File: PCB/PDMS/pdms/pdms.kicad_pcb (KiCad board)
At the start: 2 copper layers, 166 parts, among them IC1 BTS500101TAEATMA1, IC10 LDO40LPU50RY, IC11 MP2332HGTL-P, IC12 TMP126NDCKR, IC14 TMP126NDCKR, IC15 LM74700MDDFREP, IC16 BTS722204ESAXUMA1, IC19 STM32L496ZGT6, IC2 BTS500101TAEATMA1, IC20 AT25SF128A-SHB-T, IC3 BTS500101TAEATMA1, IC4 BTS500101TAEATMA1, IC5 BTS500101TAEATMA1, IC6 BTS500101TAEATMA1, IC7 BTS722204ESAXUMA1, IC8 BTS500101TAEATMA1, IC9 BTS500101TAEATMA1, J1 DBG, Q1 AO3401A, Q2 MMBT3904, Q3 IAUA250N04S6N007AUMA1, U1 CPC1117N, U2 MCP2561-E-SN, U3 MCP2561-E-SN, Y1 48Mhz, Y2 32KHz

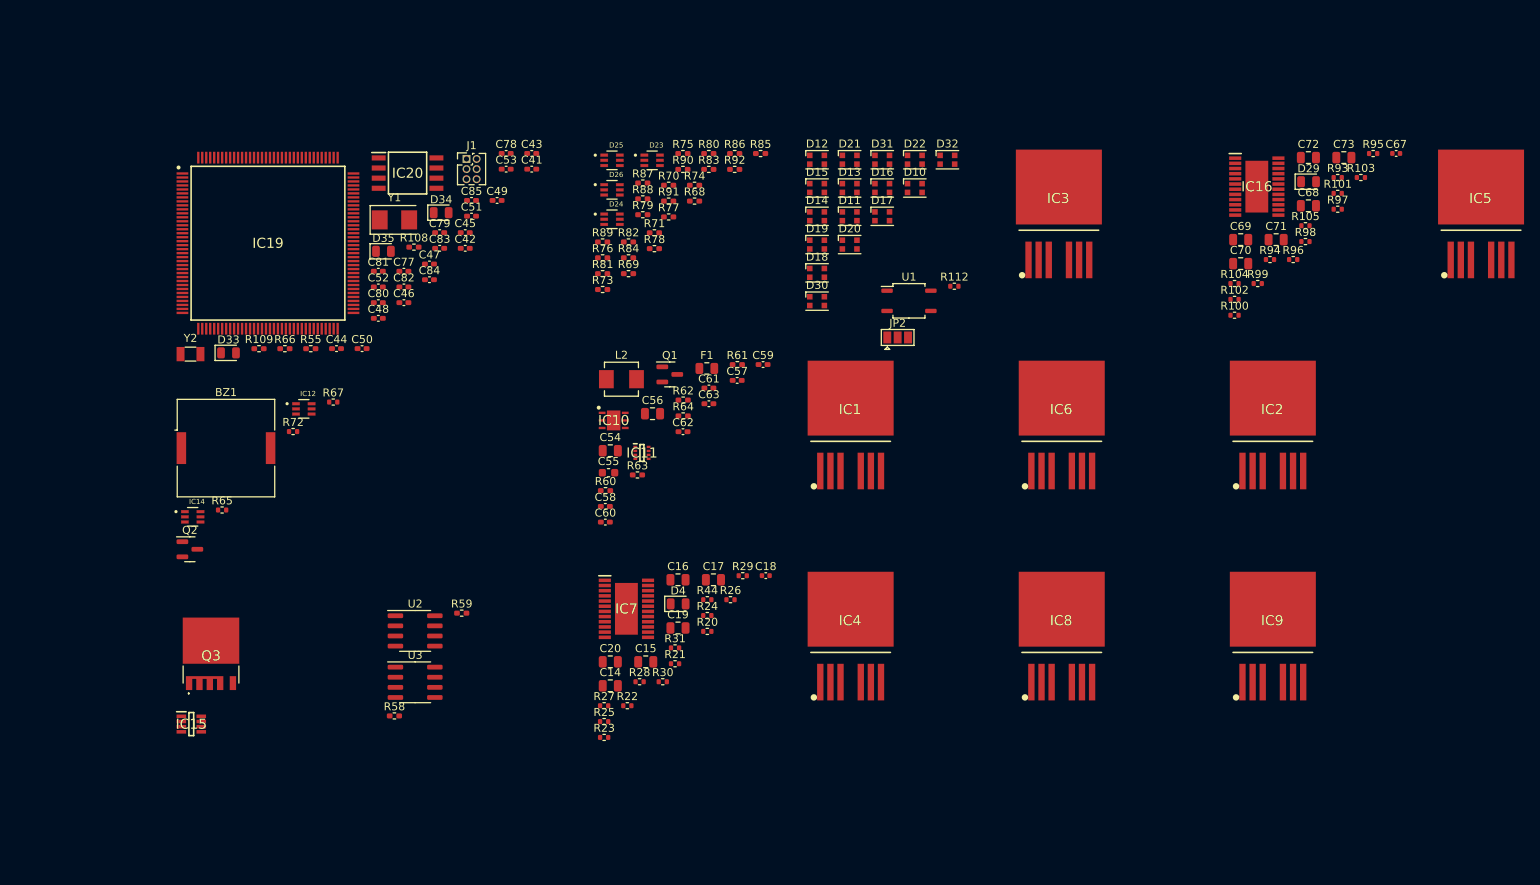
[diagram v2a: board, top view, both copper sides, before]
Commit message: Mostly assigned footprints
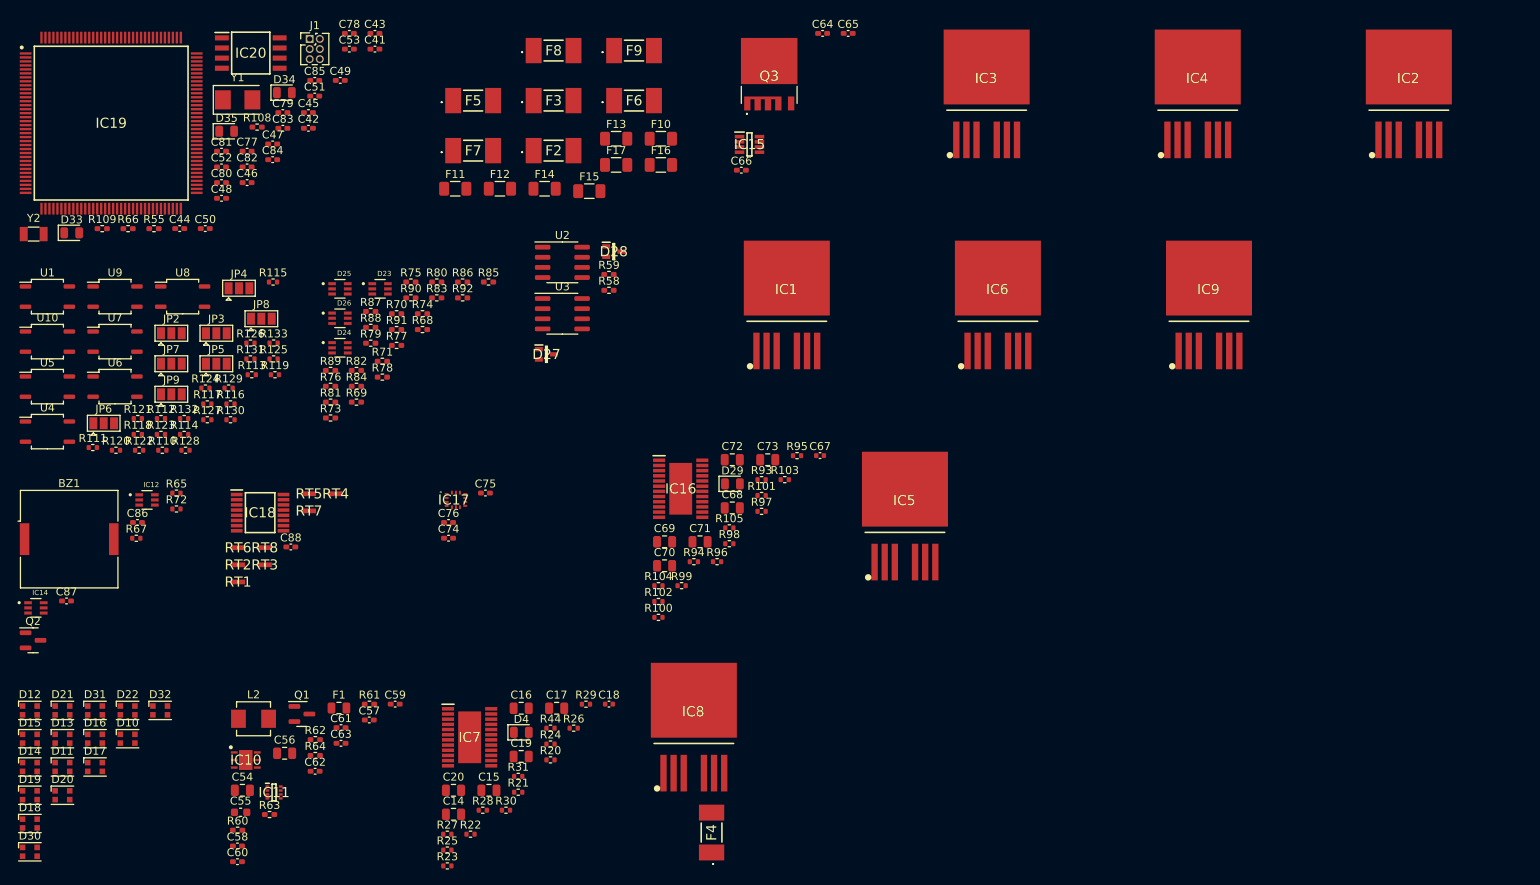
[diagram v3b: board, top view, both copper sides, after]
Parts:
- added C64: 22uF, Capacitor_SMD:C_0402_1005Metric_Pad0.74x0.62mm_HandSolder, F.Cu at (176.5, 69.9)
- added C65: 0.1uF, Capacitor_SMD:C_0402_1005Metric_Pad0.74x0.62mm_HandSolder, F.Cu at (179.7, 69.9)
- added C66: 100nF, Capacitor_SMD:C_0402_1005Metric_Pad0.74x0.62mm_HandSolder, F.Cu at (166.3, 87.0)
- added C74: 100nF, Capacitor_SMD:C_0402_1005Metric_Pad0.74x0.62mm_HandSolder, F.Cu at (129.5, 133.2)
- added C75: 10nF, Capacitor_SMD:C_0402_1005Metric_Pad0.74x0.62mm_HandSolder, F.Cu at (134.2, 127.6)
- added C76: 100nF, Capacitor_SMD:C_0402_1005Metric_Pad0.74x0.62mm_HandSolder, F.Cu at (129.5, 131.3)
- added C86: 0.1uF, Capacitor_SMD:C_0402_1005Metric_Pad0.74x0.62mm_HandSolder, F.Cu at (90.5, 131.3)
- added C87: 0.1uF, Capacitor_SMD:C_0402_1005Metric_Pad0.74x0.62mm_HandSolder, F.Cu at (81.6, 141.1)
- added C88: 100nF, Capacitor_SMD:C_0402_1005Metric_Pad0.74x0.62mm_HandSolder, F.Cu at (109.7, 134.3)
- added D27: PESD2CANFD24L-UX, PDMS_Additional:SOT65P210X110-3N, F.Cu at (141.8, 110.2)
- added D28: PESD2CANFD24L-UX, PDMS_Additional:SOT65P210X110-3N, F.Cu at (150.3, 97.2)
- added F10: 7A, Fuse:Fuse_1206_3216Metric, F.Cu at (156.2, 83.1)
- added F11: 7A, Fuse:Fuse_1206_3216Metric, F.Cu at (130.4, 89.4)
- added F12: 7A, Fuse:Fuse_1206_3216Metric, F.Cu at (136.0, 89.4)
- added F13: 7A, Fuse:Fuse_1206_3216Metric, F.Cu at (150.6, 83.1)
- added F14: 7A, Fuse:Fuse_1206_3216Metric, F.Cu at (141.6, 89.4)
- added F15: 7A, Fuse:Fuse_1206_3216Metric, F.Cu at (147.2, 89.7)
- added F16: 7A, Fuse:Fuse_1206_3216Metric, F.Cu at (156.2, 86.4)
- added F17: 7A, Fuse:Fuse_1206_3216Metric, F.Cu at (150.6, 86.4)
- added F2: 40A, PDMS_Additional:0ACA9400TE, F.Cu at (142.7, 84.6)
- added F3: 40A, PDMS_Additional:0ACA9400TE, F.Cu at (142.7, 78.3)
- added F4: 40A, PDMS_Additional:0ACA9400TE, F.Cu at (162.6, 170.2)
- added F5: 40A, PDMS_Additional:0ACA9400TE, F.Cu at (132.6, 78.3)
- added F6: 40A, PDMS_Additional:0ACA9400TE, F.Cu at (152.8, 78.3)
- added F7: 40A, PDMS_Additional:0ACA9400TE, F.Cu at (132.6, 84.6)
- added F8: 40A, PDMS_Additional:0ACA9400TE, F.Cu at (142.7, 72.0)
- added F9: 40A, PDMS_Additional:0ACA9400TE, F.Cu at (152.8, 72.0)
- added IC17: ASM330LHHTR, PDMS_Additional:LGA-14_2.5X3X0.86_, F.Cu at (130.5, 128.4)
- added IC18: NX3L4051PW,118, PDMS_Additional:SOP65P640X110-16N, F.Cu at (105.9, 130.0)
- added JP3: IN_SEL, Jumper:SolderJumper-3_P1.3mm_Open_Pad1.0x1.5mm, F.Cu at (100.4, 107.5)
- added JP4: IN_SEL, Jumper:SolderJumper-3_P1.3mm_Open_Pad1.0x1.5mm, F.Cu at (103.2, 101.8)
- added JP5: IN_SEL, Jumper:SolderJumper-3_P1.3mm_Open_Pad1.0x1.5mm, F.Cu at (100.4, 111.3)
- added JP6: IN_SEL, Jumper:SolderJumper-3_P1.3mm_Open_Pad1.0x1.5mm, F.Cu at (86.2, 118.8)
- added JP7: IN_SEL, Jumper:SolderJumper-3_P1.3mm_Open_Pad1.0x1.5mm, F.Cu at (94.7, 111.3)
- added JP8: IN_SEL, Jumper:SolderJumper-3_P1.3mm_Open_Pad1.0x1.5mm, F.Cu at (106.0, 105.7)
- added JP9: IN_SEL, Jumper:SolderJumper-3_P1.3mm_Open_Pad1.0x1.5mm, F.Cu at (94.7, 115.2)
- added R110: 0Ohm, Resistor_SMD:R_0402_1005Metric, F.Cu at (93.6, 122.2)
- added R111: 0Ohm, Resistor_SMD:R_0402_1005Metric, F.Cu at (84.9, 121.8)
- added R113: 0Ohm, Resistor_SMD:R_0402_1005Metric, F.Cu at (104.8, 112.7)
- added R114: 0Ohm, Resistor_SMD:R_0402_1005Metric, F.Cu at (96.3, 120.2)
- added R115: 0Ohm, Resistor_SMD:R_0402_1005Metric, F.Cu at (107.5, 101.1)
- added R116: 0Ohm, Resistor_SMD:R_0402_1005Metric, F.Cu at (102.2, 116.4)
- added R117: 0Ohm, Resistor_SMD:R_0402_1005Metric, F.Cu at (99.3, 116.4)
- added R118: 0Ohm, Resistor_SMD:R_0402_1005Metric, F.Cu at (90.5, 120.2)
- added R119: 0Ohm, Resistor_SMD:R_0402_1005Metric, F.Cu at (107.8, 112.7)
- added R120: 0Ohm, Resistor_SMD:R_0402_1005Metric, F.Cu at (87.8, 122.2)
- added R121: 0Ohm, Resistor_SMD:R_0402_1005Metric, F.Cu at (90.5, 118.2)
- added R122: 0Ohm, Resistor_SMD:R_0402_1005Metric, F.Cu at (90.7, 122.2)
- added R123: 0Ohm, Resistor_SMD:R_0402_1005Metric, F.Cu at (93.4, 120.2)
- added R124: 0Ohm, Resistor_SMD:R_0402_1005Metric, F.Cu at (99.0, 114.4)
- added R125: 0Ohm, Resistor_SMD:R_0402_1005Metric, F.Cu at (107.6, 110.7)
- added R126: 0Ohm, Resistor_SMD:R_0402_1005Metric, F.Cu at (104.7, 108.7)
- added R127: 1k, Resistor_SMD:R_0402_1005Metric, F.Cu at (99.3, 118.4)
- added R128: 1k, Resistor_SMD:R_0402_1005Metric, F.Cu at (96.5, 122.2)
- added R129: 1k, Resistor_SMD:R_0402_1005Metric, F.Cu at (101.9, 114.4)
- added R130: 1k, Resistor_SMD:R_0402_1005Metric, F.Cu at (102.2, 118.4)
- added R131: 1k, Resistor_SMD:R_0402_1005Metric, F.Cu at (104.7, 110.7)
- added R132: 1k, Resistor_SMD:R_0402_1005Metric, F.Cu at (96.3, 118.2)
- added R133: 1k, Resistor_SMD:R_0402_1005Metric, F.Cu at (107.6, 108.7)
- added RT1: B57232V5103F360, PDMS_Additional:THRMC1005X60N, F.Cu at (103.1, 138.7)
- added RT2: B57232V5103F360, PDMS_Additional:THRMC1005X60N, F.Cu at (103.1, 136.6)
- added RT3: B57232V5103F360, PDMS_Additional:THRMC1005X60N, F.Cu at (106.5, 136.6)
- added RT4: B57232V5103F360, PDMS_Additional:THRMC1005X60N, F.Cu at (115.4, 127.7)
- added RT5: B57232V5103F360, PDMS_Additional:THRMC1005X60N, F.Cu at (112.0, 127.7)
- added RT6: B57232V5103F360, PDMS_Additional:THRMC1005X60N, F.Cu at (103.1, 134.4)
- added RT7: B57232V5103F360, PDMS_Additional:THRMC1005X60N, F.Cu at (112.0, 129.8)
- added RT8: B57232V5103F360, PDMS_Additional:THRMC1005X60N, F.Cu at (106.5, 134.4)
- added U10: CPC1117N, Package_SO:SOP-4_3.8x4.1mm_P2.54mm, F.Cu at (79.2, 108.5)
- added U4: CPC1117N, Package_SO:SOP-4_3.8x4.1mm_P2.54mm, F.Cu at (79.2, 119.8)
- added U5: CPC1117N, Package_SO:SOP-4_3.8x4.1mm_P2.54mm, F.Cu at (79.2, 114.2)
- added U6: CPC1117N, Package_SO:SOP-4_3.8x4.1mm_P2.54mm, F.Cu at (87.7, 114.2)
- added U7: CPC1117N, Package_SO:SOP-4_3.8x4.1mm_P2.54mm, F.Cu at (87.7, 108.5)
- added U8: CPC1117N, Package_SO:SOP-4_3.8x4.1mm_P2.54mm, F.Cu at (96.2, 102.9)
- added U9: CPC1117N, Package_SO:SOP-4_3.8x4.1mm_P2.54mm, F.Cu at (87.7, 102.9)
- C14, C15, C16, C17, C70, C71, C72, C73: value 10nf -> 10nF
- F1: value Fuse -> 3A
- moved D11 120.6 mm to (81.1, 161.9)
- moved D13 120.6 mm to (81.1, 158.4)
- moved D16 120.6 mm to (85.2, 158.4)
- moved D17 120.6 mm to (85.2, 161.9)
- moved D20 120.6 mm to (81.1, 165.5)
- moved D21 120.6 mm to (81.1, 154.8)
- moved D31 120.6 mm to (85.2, 154.8)
- moved D12 120.6 mm to (77.0, 154.8)
- moved D14 120.6 mm to (77.0, 161.9)
- moved D15 120.6 mm to (77.0, 158.4)
- moved D18 120.6 mm to (77.0, 169.1)
- moved D19 120.6 mm to (77.0, 165.5)
- moved D30 120.6 mm to (77.0, 172.6)
- moved D10 120.6 mm to (89.2, 158.4)
- moved D22 120.6 mm to (89.2, 154.8)
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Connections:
- net CONN_INPUT1 renamed CONN_AD_IN1
- C54 pad 1: +12V -> 12V_LOGIC_ONLY
- C56 pad 2: +12V -> 12V_LOGIC_ONLY
- C58 pad 2: +12V -> 12V_LOGIC_ONLY
- F1 pad 1: Net-(F1-Pad1) -> 12V_LOGIC_ONLY
- IC10 pad 2: +12V -> 12V_LOGIC_ONLY
- IC10 pad 3: +12V -> 12V_LOGIC_ONLY
- IC11 pad 2: +12V -> 12V_LOGIC_ONLY
- IC12 pad 6: VDD -> Net-(C86-Pad1)
- IC14 pad 5: /PERIPHERAL/TEMP2_ALERT -> /PERIPHERAL/TEMP1_ALERT
- IC14 pad 6: VDD -> Net-(C87-Pad1)
- IC15 pad 1: /REVERSE_POLARITY_PROT/IN -> 12V_CONN
- IC15 pad 5: /REVERSE_POLARITY_PROT/IN -> 12V_CONN
- IC19 pad 118: /PERIPHERAL/TEMP2_ALERT -> /TEMP2_ALERT
- Q3 pad 1: /REVERSE_POLARITY_PROT/IN -> 12V_CONN
- Q3 pad 2: /REVERSE_POLARITY_PROT/IN -> 12V_CONN
- Q3 pad 3: /REVERSE_POLARITY_PROT/IN -> 12V_CONN
- Q3 pad 4: /REVERSE_POLARITY_PROT/IN -> 12V_CONN
- Q3 pad 7: /REVERSE_POLARITY_PROT/IN -> 12V_CONN
- R60 pad 2: +12V -> 12V_LOGIC_ONLY
- R67 pad 1: /PERIPHERAL/TEMP2_ALERT -> VDD
- R67 pad 2: VDD -> /PERIPHERAL/TEMP1_ALERT
- U1 pad 4: SIG_IN[1..8] -> SIG_IN1

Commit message: Crucial fully assigned schematics
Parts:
- added C1: 10nF, Capacitor_SMD:C_0402_1005Metric, F.Cu at (60.0, 91.2)
- added C10: 150nF, Capacitor_SMD:C_0805_2012Metric, F.Cu at (114.7, 31.0)
- added C11: 100nF, Capacitor_SMD:C_0805_2012Metric, F.Cu at (106.7, 32.5)
- added C12: 10nF, Capacitor_SMD:C_0805_2012Metric, F.Cu at (114.7, 28.0)
- added C13: 10nF, Capacitor_SMD:C_0402_1005Metric, F.Cu at (98.2, 64.7)
- added C2: 150nF, Capacitor_SMD:C_0805_2012Metric, F.Cu at (61.5, 88.7)
- added C21: 150nF, Capacitor_SMD:C_0805_2012Metric, F.Cu at (99.7, 62.2)
- added C22: 100nF, Capacitor_SMD:C_0805_2012Metric, F.Cu at (91.6, 63.8)
- added C23: 10nF, Capacitor_SMD:C_0805_2012Metric, F.Cu at (99.7, 59.2)
- added C24: 10nF, Capacitor_SMD:C_0402_1005Metric, F.Cu at (60.0, 117.7)
- added C25: 150nF, Capacitor_SMD:C_0805_2012Metric, F.Cu at (61.5, 115.2)
- added C26: 100nF, Capacitor_SMD:C_0805_2012Metric, F.Cu at (53.5, 116.8)
- added C27: 10nF, Capacitor_SMD:C_0805_2012Metric, F.Cu at (61.5, 112.2)
- added C28: 10nF, Capacitor_SMD:C_0402_1005Metric, F.Cu at (142.4, 33.5)
- added C29: 150nF, Capacitor_SMD:C_0805_2012Metric, F.Cu at (143.9, 31.0)
- added C3: 100nF, Capacitor_SMD:C_0805_2012Metric, F.Cu at (53.5, 90.3)
- added C30: 100nF, Capacitor_SMD:C_0805_2012Metric, F.Cu at (135.8, 32.5)
- added C31: 10nF, Capacitor_SMD:C_0805_2012Metric, F.Cu at (143.9, 28.0)
- added C32: 10nF, Capacitor_SMD:C_0402_1005Metric, F.Cu at (89.2, 91.2)
- added C33: 150nF, Capacitor_SMD:C_0805_2012Metric, F.Cu at (90.7, 88.7)
- added C34: 100nF, Capacitor_SMD:C_0805_2012Metric, F.Cu at (82.6, 90.3)
- added C35: 10nF, Capacitor_SMD:C_0805_2012Metric, F.Cu at (90.7, 85.7)
- added C36: 10nF, Capacitor_SMD:C_0402_1005Metric, F.Cu at (171.5, 33.5)
- added C37: 150nF, Capacitor_SMD:C_0805_2012Metric, F.Cu at (173.0, 31.0)
- added C38: 100nF, Capacitor_SMD:C_0805_2012Metric, F.Cu at (165.0, 32.5)
- added C39: 10nF, Capacitor_SMD:C_0805_2012Metric, F.Cu at (173.0, 28.0)
- added C4: 10nF, Capacitor_SMD:C_0805_2012Metric, F.Cu at (61.5, 85.7)
- added C5: 10nF, Capacitor_SMD:C_0402_1005Metric, F.Cu at (127.3, 60.0)
- added C6: 150nF, Capacitor_SMD:C_0805_2012Metric, F.Cu at (128.8, 57.5)
- added C7: 100nF, Capacitor_SMD:C_0805_2012Metric, F.Cu at (120.8, 59.0)
- added C8: 10nF, Capacitor_SMD:C_0805_2012Metric, F.Cu at (128.8, 54.5)
- added C9: 10nF, Capacitor_SMD:C_0402_1005Metric, F.Cu at (113.2, 33.5)
- added D1: 40V, Diode_SMD:D_SMA, F.Cu at (55.3, 86.5)
- added D2: 40V, Diode_SMD:D_SMA, F.Cu at (122.6, 55.2)
- added D3: 40V, Diode_SMD:D_SMA, F.Cu at (108.5, 28.7)
- added D5: 40V, Diode_SMD:D_SMA, F.Cu at (93.4, 60.0)
- added D6: 40V, Diode_SMD:D_SMA, F.Cu at (55.3, 113.0)
- added D7: 40V, Diode_SMD:D_SMA, F.Cu at (137.6, 28.7)
- added D8: 40V, Diode_SMD:D_SMA, F.Cu at (84.4, 86.5)
- added D9: 40V, Diode_SMD:D_SMA, F.Cu at (166.8, 28.7)
- added JP1: SolderJumper_3_Open, Jumper:SolderJumper-3_P1.3mm_Open_Pad1.0x1.5mm, F.Cu at (66.8, 40.0)
- added R1: 4.7k, Resistor_SMD:R_0402_1005Metric, F.Cu at (57.1, 91.7)
- added R10: 1k, Resistor_SMD:R_0805_2012Metric, F.Cu at (120.8, 62.0)
- added R106: 20k, Resistor_SMD:R_0402_1005Metric, F.Cu at (96.5, 124.9)
- added R107: 10, Resistor_SMD:R_0402_1005Metric, F.Cu at (105.4, 116.0)
- added R11: 4.7k, Resistor_SMD:R_0402_1005Metric, F.Cu at (110.3, 34.0)
- added R12: 4.7k, Resistor_SMD:R_0402_1005Metric, F.Cu at (105.9, 38.0)
- added R13: 4.7k, Resistor_SMD:R_0402_1005Metric, F.Cu at (110.3, 32.0)
- added R14: 4.7k, Resistor_SMD:R_0402_1005Metric, F.Cu at (104.2, 44.6)
- added R15: 1k, Resistor_SMD:R_0805_2012Metric, F.Cu at (106.6, 35.5)
- added R16: 4.7k, Resistor_SMD:R_0402_1005Metric, F.Cu at (95.3, 65.2)
- added R17: 4.7k, Resistor_SMD:R_0402_1005Metric, F.Cu at (90.9, 69.2)
- added R18: 4.7k, Resistor_SMD:R_0402_1005Metric, F.Cu at (95.3, 63.2)
- added R19: 4.7k, Resistor_SMD:R_0402_1005Metric, F.Cu at (89.2, 75.9)
- added R2: 4.7k, Resistor_SMD:R_0402_1005Metric, F.Cu at (52.7, 95.7)
- added R3: 4.7k, Resistor_SMD:R_0402_1005Metric, F.Cu at (57.1, 89.7)
- added R32: 1k, Resistor_SMD:R_0805_2012Metric, F.Cu at (91.6, 66.7)
- added R33: 4.7k, Resistor_SMD:R_0402_1005Metric, F.Cu at (57.1, 118.2)
- added R34: 4.7k, Resistor_SMD:R_0402_1005Metric, F.Cu at (52.7, 122.2)
- added R35: 4.7k, Resistor_SMD:R_0402_1005Metric, F.Cu at (57.1, 116.2)
- added R36: 4.7k, Resistor_SMD:R_0402_1005Metric, F.Cu at (51.0, 128.9)
- added R37: 1k, Resistor_SMD:R_0805_2012Metric, F.Cu at (53.4, 119.7)
- added R38: 4.7k, Resistor_SMD:R_0402_1005Metric, F.Cu at (139.5, 34.0)
- added R39: 4.7k, Resistor_SMD:R_0402_1005Metric, F.Cu at (135.0, 38.0)
- added R4: 4.7k, Resistor_SMD:R_0402_1005Metric, F.Cu at (51.0, 102.4)
- added R40: 4.7k, Resistor_SMD:R_0402_1005Metric, F.Cu at (139.5, 32.0)
- added R41: 4.7k, Resistor_SMD:R_0402_1005Metric, F.Cu at (133.3, 44.6)
- added R42: 1k, Resistor_SMD:R_0805_2012Metric, F.Cu at (135.8, 35.5)
- added R43: 4.7k, Resistor_SMD:R_0402_1005Metric, F.Cu at (86.3, 91.7)
- added R45: 4.7k, Resistor_SMD:R_0402_1005Metric, F.Cu at (81.8, 95.7)
- added R46: 4.7k, Resistor_SMD:R_0402_1005Metric, F.Cu at (86.3, 89.7)
- added R47: 4.7k, Resistor_SMD:R_0402_1005Metric, F.Cu at (80.1, 102.4)
- added R48: 1k, Resistor_SMD:R_0805_2012Metric, F.Cu at (82.6, 93.2)
- added R49: 4.7k, Resistor_SMD:R_0402_1005Metric, F.Cu at (168.6, 34.0)
- added R5: 1k, Resistor_SMD:R_0805_2012Metric, F.Cu at (53.4, 93.2)
- added R50: 4.7k, Resistor_SMD:R_0402_1005Metric, F.Cu at (164.2, 38.0)
- added R51: 4.7k, Resistor_SMD:R_0402_1005Metric, F.Cu at (168.6, 32.0)
- added R52: 4.7k, Resistor_SMD:R_0402_1005Metric, F.Cu at (162.5, 44.6)
- added R53: 1k, Resistor_SMD:R_0805_2012Metric, F.Cu at (164.9, 35.5)
- added R6: 4.7k, Resistor_SMD:R_0402_1005Metric, F.Cu at (124.5, 60.5)
- added R7: 4.7k, Resistor_SMD:R_0402_1005Metric, F.Cu at (120.0, 64.5)
- added R8: 4.7k, Resistor_SMD:R_0402_1005Metric, F.Cu at (124.5, 58.5)
- added R9: 4.7k, Resistor_SMD:R_0402_1005Metric, F.Cu at (118.3, 71.1)
- moved C16 149.0 mm to (217.3, 28.0)
- moved C18 149.0 mm to (228.3, 27.5)
- moved R20 149.0 mm to (221.0, 34.5)
- moved R21 149.0 mm to (216.9, 38.5)
- moved R23 149.0 mm to (208.0, 47.8)
- moved R26 149.0 mm to (223.9, 30.5)
- moved R44 149.0 mm to (221.0, 30.5)
- moved C14 149.0 mm to (208.8, 41.3)
- moved C15 149.0 mm to (213.3, 38.3)
- moved C17 149.0 mm to (221.8, 28.0)
- moved C19 149.0 mm to (217.3, 34.0)
- moved C20 149.0 mm to (208.8, 38.3)
- moved D4 149.0 mm to (217.3, 31.0)
- moved IC7 149.0 mm to (210.8, 31.6)
- moved R22 149.0 mm to (210.9, 43.8)
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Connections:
- net /POWER_SWITCHES/BTS50010-1TAE/MOS_OUT renamed Net-(C4-Pad1)
- net /POWER_SWITCHES/BTS50010-1TAE1/MOS_OUT renamed Net-(C8-Pad1)
- net /POWER_SWITCHES/BTS50010-1TAE2/MOS_OUT renamed Net-(C12-Pad1)
- net /POWER_SWITCHES/BTS50010-1TAE3/MOS_OUT renamed Net-(C23-Pad1)
- net /POWER_SWITCHES/BTS50010-1TAE4/MOS_OUT renamed Net-(C27-Pad1)
- net /POWER_SWITCHES/BTS50010-1TAE5/MOS_OUT renamed Net-(C39-Pad1)
- net /POWER_SWITCHES/BTS50010-1TAE6/MOS_OUT renamed Net-(C31-Pad1)
- net /POWER_SWITCHES/BTS50010-1TAE7/MOS_OUT renamed Net-(C35-Pad1)

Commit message: Added connector and more
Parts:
- added J2: 6473427-1, PDMS_Additional:64734271, F.Cu at (112.1, 52.6)
- added L1: 2u7 120m, Inductor_SMD:L_0402_1005Metric, F.Cu at (69.8, 131.2)
- added R54: 0, Resistor_SMD:R_0805_2012Metric, F.Cu at (68.6, 126.8)
- added R56: 10k, Resistor_SMD:R_0402_1005Metric, F.Cu at (38.9, 176.6)
- added R57: 10k, Resistor_SMD:R_0402_1005Metric, F.Cu at (52.9, 160.5)
- C41, C42, C43, C44, C45, C46, C47, C48, C49, C50, C51, C52, C53, C57, C58, C59, C60, C61, C62, C63, C65: footprint Capacitor_SMD:C_0402_1005Metric_Pad0.74x0.62mm_HandSolder -> Resistor_SMD:R_0402_1005Metric
- C64, C66: footprint Capacitor_SMD:C_0402_1005Metric_Pad0.74x0.62mm_HandSolder -> Capacitor_SMD:C_0805_2012Metric
- R108, R109, R55, R58, R59, R60, R61, R62, R63, R64, R66, R68, R69, R70, R71, R73, R74, R75, R76, R77, R78, R79, R80, R81, R82, R83, R84, R85, R86, R87, R88, R89, R90, R91, R92: footprint Resistor_SMD:R_0402_1005Metric_Pad0.72x0.64mm_HandSolder -> Resistor_SMD:R_0402_1005Metric
- moved R1 299.9 mm to (356.9, 81.9)
- moved R4 296.6 mm to (347.3, 89.4)
- moved R2 296.3 mm to (348.9, 86.4)
- moved C2 291.8 mm to (353.2, 82.4)
- moved C3 291.8 mm to (345.2, 86.9)
- moved D1 291.8 mm to (347.0, 83.1)
- moved F2 291.8 mm to (336.2, 101.2)
- moved R5 290.1 mm to (343.5, 99.5)
- moved R3 287.3 mm to (344.4, 89.4)
- moved C1 284.4 mm to (344.4, 91.4)
- moved C4 272.6 mm to (333.4, 105.8)
- moved R49 244.0 mm to (395.6, 123.5)
- moved R53 241.5 mm to (382.2, 141.1)
- moved R10 241.1 mm to (299.1, 224.3)
- moved R50 240.8 mm to (387.6, 128.0)
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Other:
- copper layers 2 -> 4
